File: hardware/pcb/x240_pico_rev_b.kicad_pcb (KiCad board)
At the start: 2 copper layers, 100 x 80 mm, 42 parts, among them J1 FH12-40S keyboard FPC, J2 FH12-12S ClickPad FPC, J3 J_KB FPC lines 1-40, J4 J_MAT drive/sense/aux, J5 J_TP ClickPad lines 1-12, J6 J_PS2 bus/aux, J7 J_USBC TP1/TP2/TP3/VBUS, J8 J_LED 3V3/GP28R/GND, Q1 2N7002, SW1 RESET, U1 Raspberry_Pi_Pico, U2 74HC165, U3 74HC165, U4 74HC165

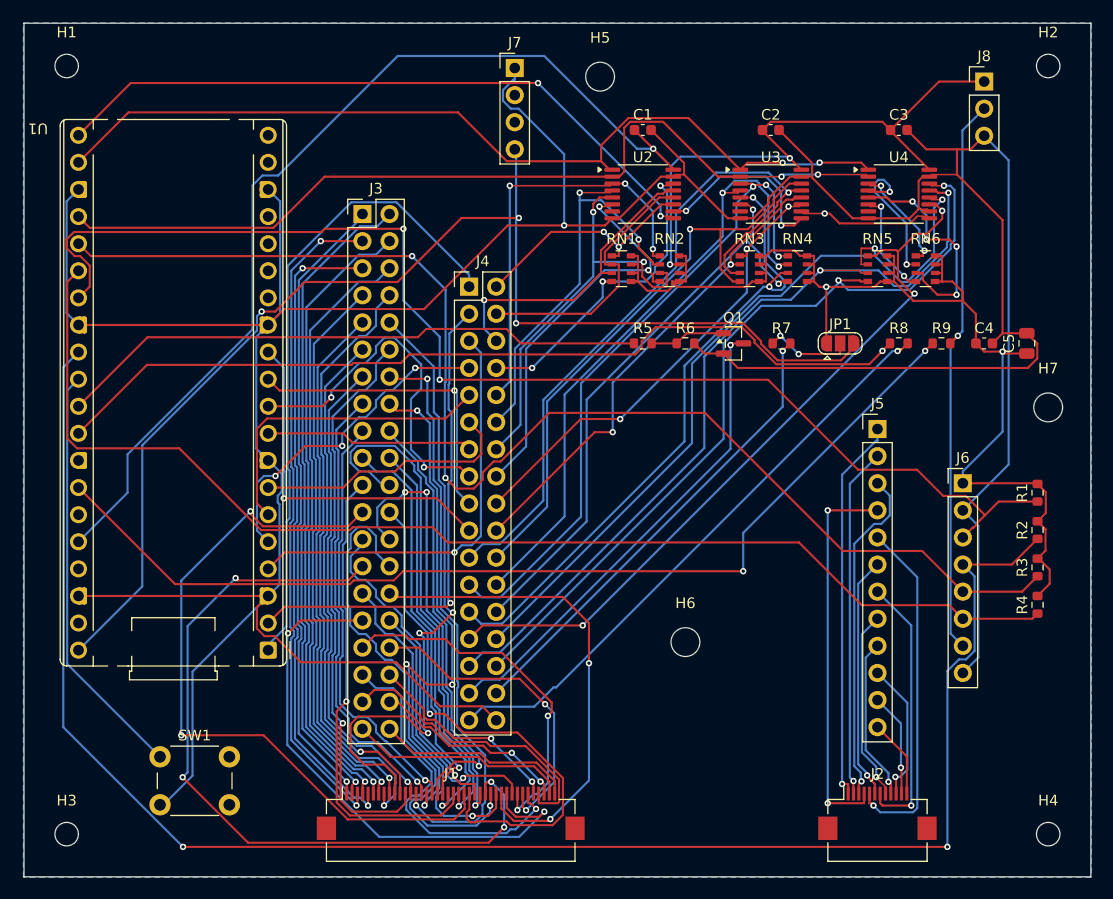
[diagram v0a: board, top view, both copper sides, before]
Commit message: dev: re-route until DRC reports no open connections
Freerouting is nondeterministic and the SES round-trip occasionally drops
a connection (CI saw 10 open after a routing pass that freerouting called
complete). build pcb now loops export -> route -> import -> DRC up to
three times, re-routing only what is still open, and prints the open pairs
when a round falls short. Board re-routed by this run.
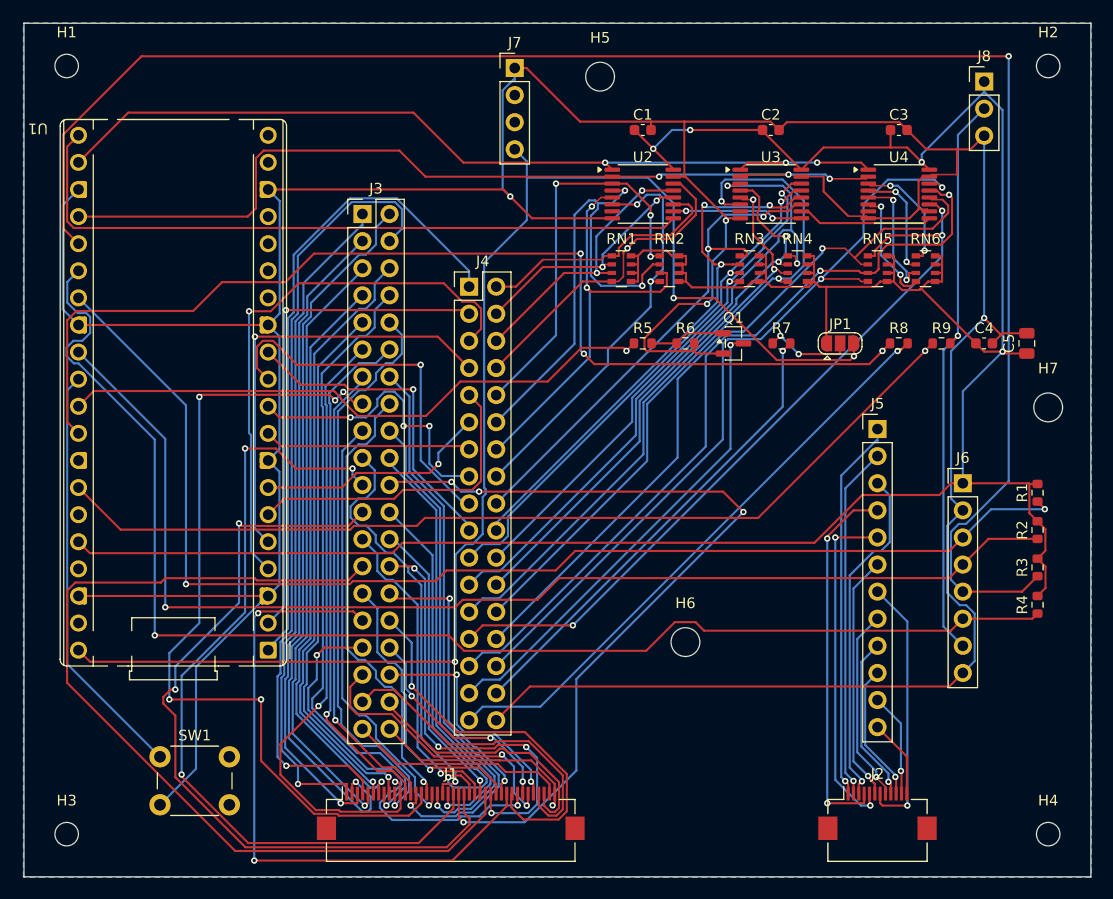
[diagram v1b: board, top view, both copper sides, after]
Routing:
- net PS2_CLK: track 159.6 -> 111.7 mm, vias 2 -> 1
- net PS2B_DATA: track 120.7 -> 163.4 mm, vias 2 -> 1
- net KB15: track 42.4 -> 78.8 mm, vias 1 -> 5
- net KB21: track 43.8 -> 76.8 mm, vias 1 -> 3
- net KB22: track 48.5 -> 80.6 mm, vias 1 -> 4
- net KB30: track 46.2 -> 26.6 mm
- net GP27: track 83.0 -> 101.2 mm, vias 1 -> 3
- net SENSE10: track 66.8 -> 49.7 mm, vias 1 -> 2
- net KB4: track 59.0 -> 73.5 mm
- net VBUS: track 117.3 -> 131.8 mm
- net KB24: track 51.1 -> 37.0 mm
- net KB26: track 41.5 -> 27.6 mm, vias 3 -> 1
- net KB27: track 72.8 -> 86.5 mm, vias 4 -> 0
- net DRV2: track 40.0 -> 52.2 mm
- net PS2B_CLK: track 114.5 -> 126.5 mm, vias 0 -> 1
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
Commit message: dev: placement DRC and exhausted routing now fail the build; docs match the verb
Copilot review on #61. The placement DRC step's fallback returned 0 whenever
violations were found; it now parses the JSON report and fails on any
error-severity violation (open connections are expected on an unrouted
board). If connections are still open after the third routing round the
build stops instead of exporting fab files. Docs: X240_ROUTE_PASSES
defaults to 100, and the BOM is bom.csv, not an interactive HTML BOM.
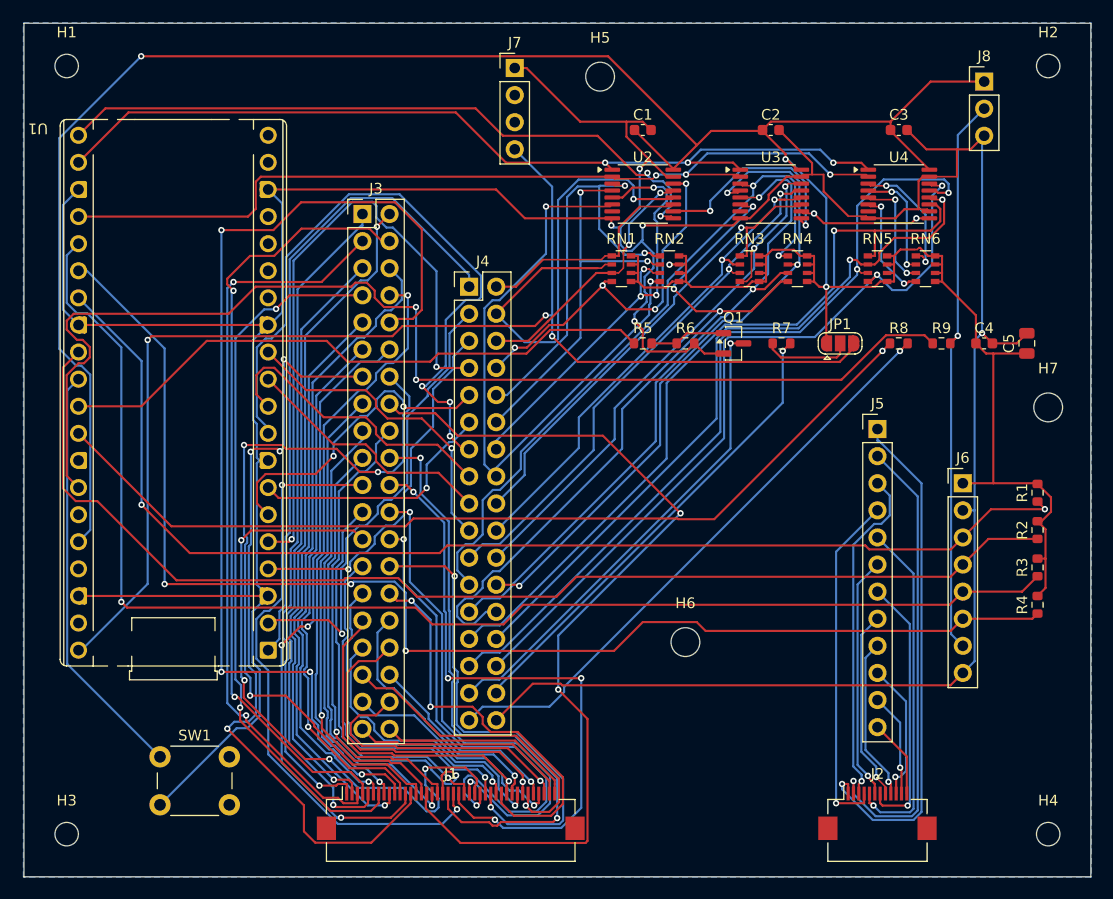
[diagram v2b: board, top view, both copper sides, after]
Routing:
- net KB27: track 86.5 -> 33.3 mm, vias 0 -> 1
- net DRV6: track 19.5 -> 64.5 mm, vias 0 -> 3
- net KB10: track 54.3 -> 98.1 mm, vias 1 -> 4
- net KB16: track 42.5 -> 86.1 mm, vias 1 -> 2
- net PS2B_DATA: track 163.4 -> 125.3 mm
- net KB23: track 73.9 -> 36.4 mm, vias 2 -> 1
- net KB15: track 78.8 -> 44.5 mm, vias 5 -> 1
- net KB25: track 30.0 -> 60.7 mm, vias 1 -> 4
- net KB31: track 60.5 -> 30.2 mm, vias 2 -> 1
- net KB13: track 43.9 -> 73.5 mm, vias 1 -> 4
- net SENSE1: track 22.8 -> 45.9 mm, vias 2 -> 1
- net GP28: track 88.9 -> 111.3 mm, vias 1 -> 2
- net SENSE7: track 38.7 -> 59.9 mm
- net KB26: track 27.6 -> 48.2 mm, vias 1 -> 2
- net KB22: track 80.6 -> 60.1 mm
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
